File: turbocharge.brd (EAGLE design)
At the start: 56.2 x 21 mm, 69 parts, among them Q01 NMOS40V_10A, Q03 NMOS40V_10A, Q11 PMOS30V_11A, Q12 PMOS30V_11A, Q13 2PMOS30V_2A, Q15 PMOS30V_11A, Q16 PMOS30V_11A, Q21 PMOS30V_11A, Q22 PMOS30V_11A, Q23 PMOS30V_11A, Q25 PMOS30V_11A, Q26 PMOS30V_11A, Q27 PMOS30V_11A, Q28 PMOS30V_11A, Q31 PMOS30V_11A, Q32 PMOS30V_11A, Q33 PMOS30V_11A, Q34 PMOS30V_11A, Q35 PMOS30V_11A, Q36 PMOS30V_11A, Q37 PMOS30V_11A, Q38 PMOS30V_11A, Q41 PMOS30V_11A, Q42 PMOS30V_11A, Q43 PMOS30V_11A, Q44 PMOS30V_11A, Q45 PMOS30V_11A, Q46 PMOS30V_11A, Q47 PMOS30V_11A, Q48 PMOS30V_11A, Q51 PMOS30V_11A, Q52 PMOS30V_11A, Q53 PMOS30V_11A, Q54 PMOS30V_11A, Q55 PMOS30V_11A, Q56 PMOS30V_11A, Q57 PMOS30V_11A, Q58 PMOS30V_11A, Q62 PMOS30V_11A, Q64 PMOS30V_11A, Q66 PMOS30V_11A, Q68 PMOS30V_11A, U1 ATTINY13A10M1, U2 DG408DVZ, U3 CCR20MA_45V

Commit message: .
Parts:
- removed D4, DG1: 4DSCH30V_0A1, dubec:8-HMD
- removed R11, R12: RES100K_16, dubec:0402
- added D6: 3D_SCHOTTKY30V_0.35V, dubec:SOT-363
- added Q17: 2PMOS50V_0.17A, dubec:SOT-666
- added RG11, RG21-: RES100K_16, dubec:0402
- D2: value 3D_SCHOTTKY30V_0.35V -> 4DSCH30V_0A1; device dubec:SOT-363 -> dubec:8-HMD
- Q11, Q12, Q23: value PMOS30V_11A -> NMOS40V_10A
- Q13: value 2PMOS30V_2A -> NMOS40V_10A; device dubec:6-TSOP -> dubec:6-POWERWDFN
- moved D2 66.6 mm to (4.40, 14.8), turned to 0 degrees
- moved Q13 50.5 mm to (21.1, 2.60), turned to 180 degrees
- moved Q01 28.2 mm to (0.00, -16.0), turned to 0 degrees
- moved Q23 26.5 mm to (0.00, -13.8), turned to 0 degrees
- moved Q15 8.00 mm to (17.2, 5.10)
- moved Q16 7.88 mm to (19.9, 5.10)
- moved Q32 2.07 mm to (13.7, 10.5)
- moved Q52 2.07 mm to (13.7, 15.5)
- moved Q31 2.00 mm to (11.0, 10.5)
- moved Q51 2.00 mm to (11.0, 15.5)
- moved Q12 0.57 mm to (13.7, 5.50)
- moved Q22 0.07 mm to (13.7, 8.00)
- moved Q42 0.07 mm to (13.7, 13.0)
- moved Q62 0.07 mm to (13.7, 18.0)
- renumbered RG21 to RG21+, U$2 to T1
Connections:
- removed net G21: D3.5, DG1.7, Q21.G, Q22.G, Q23.G, RG21+.2, U2.6
- removed net N$17: Q12.G, Q13.6, R12.2
- removed net N$18: DG1.1, DG1.2, Q11.G
- new net C4+: D1.4, D1.6, D1.7, D1.8, Q17.1, RG11.1
- new net G21+: D3.5, Q17.2, Q21.G, Q22.G, RG21+.2, U2.6
- new net G21-: Q01.G, Q17.6, Q23.G, RG21-.2
- new net S+11: Q11.S, Q12.S
- net BATT+: now also D2.5, D2.6; no longer D1.6, D1.7, D1.8, D4.6
- net BATT-: now also Q13.S, RG21-.1; no longer Q01.S, R12.1
- net C1: now also Q17.4, Q23.D; no longer Q13.2, Q13.5
- net C2: no longer R11.1
- net C5: now also D2.4; no longer D1.4
- net C6: now also D2.3; no longer D4.3
- net G02: now also Q17.3; no longer Q13.4
- net G11: now also Q11.G, Q12.G, Q13.G, RG11.2; no longer DG1.8, Q01.G, Q13.1, R11.2
- net G13: now also Q17.5; no longer Q13.3
- net G41: now also D6.4; no longer D2.4
- net G51: now also D6.5; no longer D2.5
- net G61: now also D6.6; no longer D2.6
- net N$12: now also D6.2; no longer D2.2
- net N$13: now also D6.3; no longer D2.3
- net N$8: now also D6.1; no longer D2.1
- net S+: now also D2.1, D2.2; no longer D4.1, D4.2
- net S-: now also Q13.D; no longer Q23.D
- net S-21: now also Q01.S; no longer Q11.S, Q12.S
- net VCC: now also D2.7, D2.8; no longer D4.7, D4.8
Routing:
- net S+: track 0.00 -> 12.5 mm
- net C6: track 0.00 -> 4.97 mm
- net S-21: track 3.25 -> 0.00 mm, vias 4 -> 0
- net C5: track 0.00 -> 2.70 mm
- net C4: track 0.00 -> 2.70 mm
- net C3: track 0.00 -> 2.70 mm
- net C2: track 0.00 -> 2.70 mm
- net C1: track 0.00 -> 2.70 mm
- net G51: track 0.00 -> 1.00 mm
- net G41: track 0.00 -> 1.00 mm
- net G31: track 0.00 -> 1.00 mm
- net G21+: track 0.00 -> 1.00 mm, vias 0 -> 2
- net G11: track 0.00 -> 1.00 mm, vias 0 -> 2
- net G61: track 0.00 -> 0.50 mm, vias 2 -> 1
- net N$18: track 0.48 -> 0.00 mm, vias 1 -> 0
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
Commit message: Modularizing next
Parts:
- moved Q15 1.01 mm to (16.3, 5.50)
- moved Q16 0.89 mm to (19.1, 5.50)
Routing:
- net C1: track 2.70 -> 14.6 mm, vias 0 -> 3
- net G21+: track 1.00 -> 3.00 mm
- net G41: track 1.00 -> 3.00 mm
- net G31: track 1.00 -> 3.00 mm
- net G51: track 1.00 -> 3.00 mm
- net G11: track 1.00 -> 2.36 mm
- net S+11: track 0.00 -> 1.28 mm
- added copper zone on layer 15, net BATT-
- added copper zone on layer 2, net BATT-

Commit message: .
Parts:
- moved Q01 29.8 mm to (20.7, 5.50), turned to 180 degrees
- moved Q23 26.4 mm to (18.0, 5.50)
- moved RG21- 26.0 mm to (12.2, 2.60)
- moved RG11 24.0 mm to (4.40, 5.40)
- moved Q15 9.00 mm to (25.3, 5.50)
- moved Q16 9.00 mm to (28.1, 5.50)
- moved R1 2.01 mm to (17.2, 2.60)
- moved Q33 0.72 mm to (18.0, 8.00)
- moved Q43 0.72 mm to (18.0, 10.5)
- moved Q53 0.72 mm to (18.0, 13.0)
- moved Q34 0.62 mm to (20.7, 8.00)
- moved Q44 0.62 mm to (20.7, 10.5)
- moved Q54 0.62 mm to (20.7, 13.0)
- moved Q64 0.62 mm to (20.7, 15.5)
- moved Q13 0.62 mm to (20.7, 3.00)
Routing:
- net C1: track 14.6 -> 23.6 mm
- net G11: track 2.36 -> 3.00 mm

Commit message: .
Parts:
- removed D3, D6: 3D_SCHOTTKY30V_0.35V, dubec:SOT-363
- removed Q01, Q03, Q13: NMOS40V_10A, dubec:6-POWERWDFN
- removed Q15: PMOS30V_11A, dubec:6-POWERWDFN
- removed Q17: 2PMOS50V_0.17A, dubec:SOT-666
- removed R7: RES100K_16, dubec:0402
- removed U2: DG408DVZ, dubec:16-TSSOP
- added Q1, Q14, Q18, Q2, Q24: NMOS40V_10A, dubec:6-POWERWDFN
- added RGT+2, RGT-2, RGT1, RGT3, RGT4, RGT5, RGT6: RES100K_16, dubec:0402
- added U$2, U$3, U$4, U$5, U$6, U$7, U4: 2NMOS30V_0.1A, dubec:SOT-666
- Q16: value PMOS30V_11A -> 2PMOS50V_0.17A; device dubec:6-POWERWDFN -> dubec:SOT-666
- Q27, Q28: value PMOS30V_11A -> NMOS40V_10A
- moved Q16 43.1 mm to (69.8, 16.2), turned to 0 degrees
- moved Q27 4.02 mm to (27.2, 5.50)
- moved Q37 4.02 mm to (27.2, 8.00)
- moved Q47 4.02 mm to (27.2, 10.5)
- moved Q57 4.02 mm to (27.2, 13.0)
- moved Q28 3.90 mm to (29.9, 5.50)
- moved Q38 3.90 mm to (29.9, 8.00)
- moved Q48 3.90 mm to (29.9, 10.5)
- moved Q58 3.90 mm to (29.9, 13.0)
- moved Q68 3.90 mm to (29.9, 15.5)
- moved Q25 3.42 mm to (21.8, 8.00)
- moved Q35 3.42 mm to (21.8, 10.5)
- moved Q45 3.42 mm to (21.8, 13.0)
- moved Q55 3.42 mm to (21.8, 15.5)
- moved Q26 3.30 mm to (24.5, 8.00)
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- renumbered RG11 to RGS1, RG21+ to RGS+2, RG21- to RGS-2, RG31 to RGS3, RG41 to RGS4, RG51 to RGS5, RG61 to RGS6
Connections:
- net S+11 renamed SS+1
- net S+21 renamed SS+2
- net S+22 renamed ST+2
- net S+31 renamed SS+3
- net S+32 renamed ST+3
- net S+41 renamed SS+4
- net S+42 renamed ST+4
- net S+51 renamed SS+5
- net S+52 renamed ST+5
- net S-22 renamed ST-2
- net S-31 renamed SS-3
- net S-32 renamed ST-3
- net S-41 renamed SS-4
- net S-42 renamed ST-4
- net S-51 renamed SS-5
- net S-52 renamed ST-5
- removed net G02: Q03.G, Q17.3, R7.2
- removed net G11: D3.4, Q11.G, Q12.G, Q13.G, RGS1.2, U2.5
- removed net G13: Q15.G, Q16.G, Q17.5
- removed net G21+: D3.5, Q17.2, Q21.G, Q22.G, RGS+2.2, U2.6
- removed net G21-: Q01.G, Q17.6, Q23.G, RGS-2.2
- removed net G22: Q25.G, Q26.G, Q27.G, Q28.G
- removed net G31: D3.6, Q31.G, Q32.G, Q33.G, Q34.G, RGS3.2, U2.7
- removed net G32: Q35.G, Q36.G, Q37.G, Q38.G
- removed net G41: D6.4, Q41.G, Q42.G, Q43.G, Q44.G, RGS4.2, U2.12
- removed net G42: Q45.G, Q46.G, Q47.G, Q48.G
- removed net G51: D6.5, Q51.G, Q52.G, Q53.G, Q54.G, RGS5.2, U2.11
- removed net G52: Q55.G, Q56.G, Q57.G, Q58.G
- removed net G61: D6.6, Q62.G, Q64.G, RGS6.2, U2.10
- removed net G62: Q66.G, Q68.G
- removed net N$10: U2.16
- removed net N$11: U2.1
- removed net N$12: D51.C, D6.2
- removed net N$8: D6.1, D61.C
- removed net N$9: U2.15
- removed net S+12: Q15.S, Q16.S
- removed net S-21: Q01.S, Q23.S
- new net !EN_S1: U4.5
- new net EN_S2: U4.2
- new net EN_S3: U$2.2
- new net EN_S4: U$2.5
- new net EN_S5: U$3.2
- new net EN_S6: U$3.5
- new net EN_T1: U$4.2
- new net EN_T2: U$4.5, U$5.2
- new net EN_T3: U$5.5
- new net EN_T4: U$6.2
- new net EN_T5: U$6.5
- new net EN_T6: U$7.2
- new net GS+2: Q16.2, Q21.G, Q22.G, RGS+2.2, U4.6
- new net GS-2: Q16.6, Q23.G, Q24.G, RGS-2.2
- new net GS1: Q11.G, Q12.G, Q14.G, RGS1.2, U4.3
- new net GS3: Q31.G, Q32.G, Q33.G, Q34.G, RGS3.2, U$2.6
- new net GS4: Q41.G, Q42.G, Q43.G, Q44.G, RGS4.2, U$2.3
- new net GS5: Q51.G, Q52.G, Q53.G, Q54.G, RGS5.2, U$3.6
- new net GS6: Q62.G, Q64.G, RGS6.2, U$3.3
- new net GT+2: Q25.G, Q26.G, RGT+2.2, U$5.6
- new net GT-2: Q27.G, Q28.G, RGT-2.2, U$4.4
- new net GT1: Q1.G, Q18.G, Q2.G, RGT1.2, U$4.1
- new net GT3: Q35.G, Q36.G, Q37.G, Q38.G, RGT3.2, U$5.3
- new net GT4: Q45.G, Q46.G, Q47.G, Q48.G, RGT4.2, U$6.6
- new net GT5: Q55.G, Q56.G, Q57.G, Q58.G, RGT5.2, U$6.3
- new net GT6: Q66.G, Q68.G, RGT6.2, U$7.6
- new net SS-2: Q23.S, Q24.S
- new net ST+1: Q1.S, Q2.S
- net BATT+: now also RGT+2.1, RGT3.1, RGT4.1, RGT5.1, RGT6.1; no longer U2.13
- net BATT-: now also Q14.S, Q18.S, RGT-2.1, RGT1.1, U$2.1, U$2.4, U$3.1, U$3.4, U$5.1, U$5.4, U$6.1, U$6.4, U$7.1, U4.1, U4.4; no longer Q03.S, Q13.S, R7.1, U2.4
- net C1: now also Q1.D; no longer Q15.D, Q17.4
- net C4+: now also Q16.1, U$4.3, U$4.6; no longer Q17.1
- net N$13: no longer D6.3
- net N$14: no longer D3.1
- net N$15: no longer D3.2
- net N$16: no longer D3.3
- net S-: now also Q14.D, Q24.D; no longer Q01.D, Q13.D
- net T+: now also Q2.D; no longer Q16.D
- net T-: now also Q18.D; no longer Q03.D
- net VCC: no longer U2.2
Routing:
- net C1: track 23.6 -> 33.3 mm, vias 3 -> 9
- net G11: track 3.00 -> 0.00 mm, vias 2 -> 0
- net GS1: track 0.00 -> 3.00 mm, vias 0 -> 2
- net G21+: track 3.00 -> 0.00 mm, vias 2 -> 0
- net GS-2: track 0.00 -> 3.00 mm, vias 0 -> 2
- net G41: track 2.60 -> 0.00 mm, vias 2 -> 0
- net G31: track 2.60 -> 0.00 mm, vias 2 -> 0
- net G51: track 2.60 -> 0.00 mm, vias 2 -> 0
- net GS4: track 0.00 -> 1.91 mm, vias 0 -> 2
- net GS3: track 0.00 -> 1.91 mm, vias 0 -> 2
- net GS+2: track 0.00 -> 1.91 mm, vias 0 -> 2
- net GS5: track 0.00 -> 1.91 mm, vias 0 -> 2
- net SS-2: track 0.00 -> 1.27 mm
- net G61: track 0.50 -> 0.00 mm, vias 1 -> 0

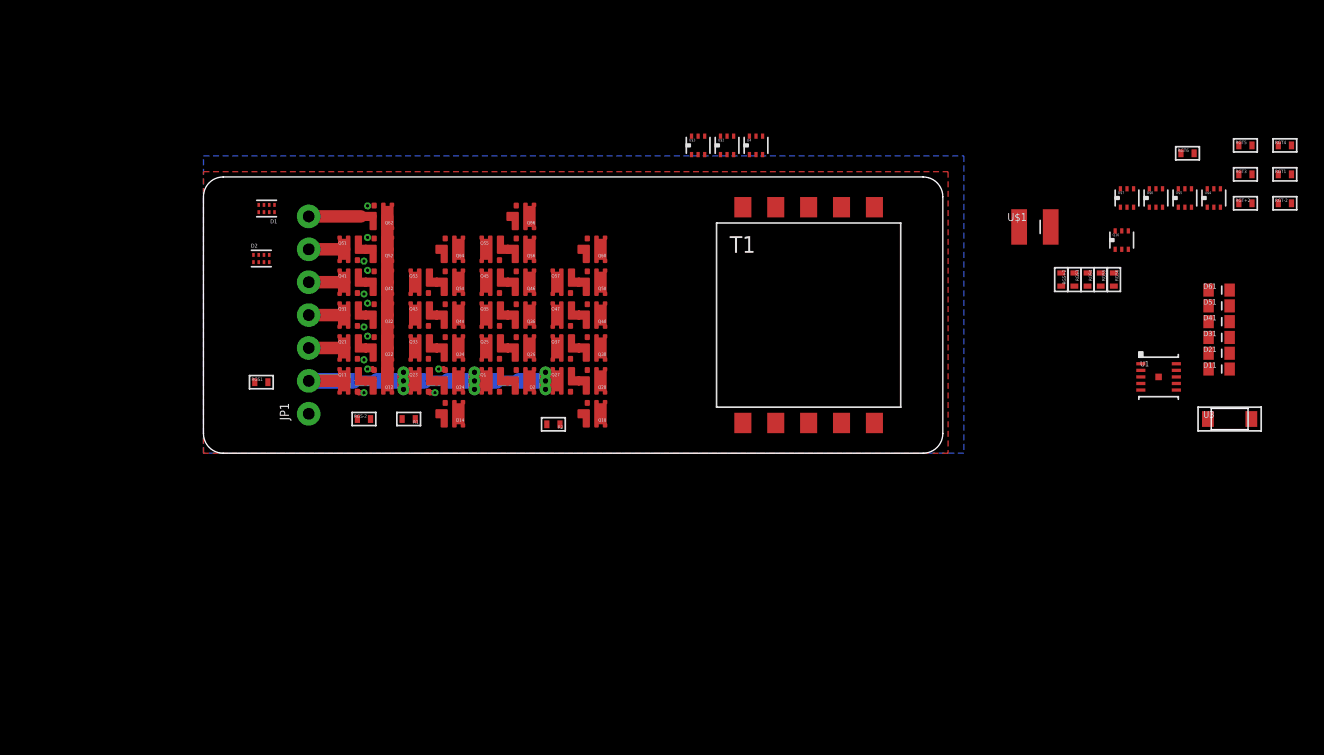
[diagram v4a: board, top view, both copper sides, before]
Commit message: Switching back to an analog switch
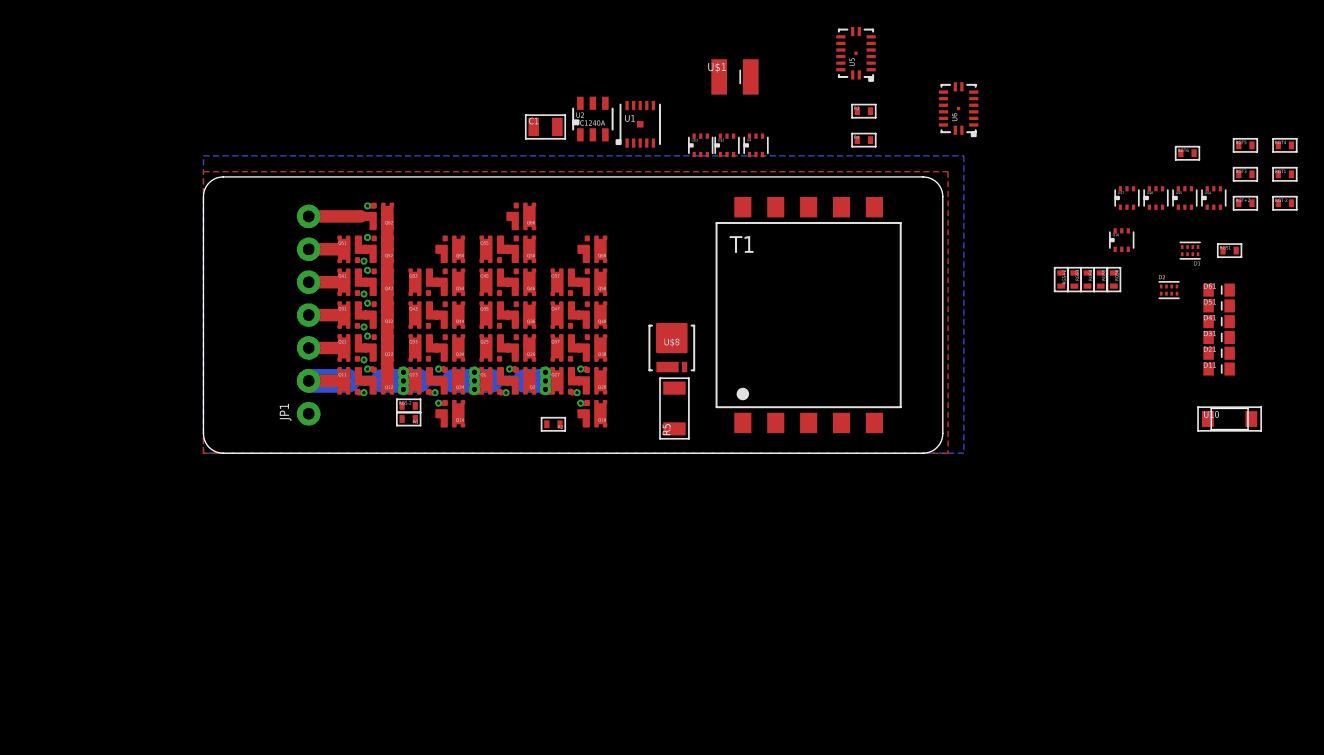
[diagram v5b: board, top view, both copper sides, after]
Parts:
- added C1: (no value), dubec:0805
- added R3, R4: RES4.7K_16, dubec:0402
- added R5: RES01_0.75W, dubec:1206
- added U$8: NMOS30V_30A, dubec:8-POWERWDFN
- added U2: TC1240A, dubec:SOT-23-6
- added U5, U6: 74HC595, dubec:16-VFQFN
- U1: value ATTINY13A10M1 -> LT3757IDD; device dubec:10-MLF -> dubec:10-WFDFN
- moved RGS1 74.3 mm to (78.0, 15.4)
- moved D1 70.3 mm to (75.0, 15.4)
- moved D2 69.0 mm to (73.4, 12.4)
- moved U1 43.8 mm to (33.2, 25.0)
- moved U$1 25.5 mm to (40.4, 28.6)
- moved RGS-2 3.54 mm to (15.6, 3.60)
- moved U$3 0.20 mm to (37.8, 23.4)
- renumbered U3 to U10
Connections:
- net N$2 renamed FBX
- removed net N$6: U1.7
- new net !OE: R3.2, U5.13, U6.13
- new net !RESET: R4.2, U5.10, U6.10
- new net CP: U5.11, U5.12, U6.11, U6.12
- new net DSS: U5.14
- new net DST: U5.9, U6.14
- new net N$10: T1.6, T1.7, U$8.D
- new net N$11: U1.10, U1.8, U1.9, U2.5
- new net N$19: U6.9
- new net N$2: U5.6
- new net N$20: U5.7
- new net N$8: C1.2, U2.6
- new net N$9: C1.1, U2.3
- new net T~: T1.3
- net !EN_S1: now also U5.15
- net BATT-: now also R4.1, U$1.C, U5.8, U5.PAD, U6.8, U6.PAD
- net C1: now also D2.1, D2.2
- net EN_S2: now also U5.1
- net EN_S3: now also U5.2
- net EN_S4: now also U5.3
- net EN_S5: now also U5.4
- net EN_S6: now also U5.5
- net EN_T1: now also U6.15
- net EN_T2: now also U6.1
- net EN_T3: now also U6.2
- net EN_T4: now also U6.3
- net EN_T5: now also U6.4
- net EN_T6: now also U6.5
- net N$1: now also U6.7; no longer U1.4
- net N$3: now also U6.6; no longer U1.1
- net N$5: now also U$8.G, U1.7; no longer U1.9
- net N$7: now also R5.2, U$8.S
- net S+: now also T1.10, T1.9, U2.1; no longer D2.1, D2.2
- net S-: now also R5.1, U1.PAD, U2.2, U2.4; no longer U$1.C, U1.11
- net T-: now also T1.1, T1.4
- net VCC: now also R3.1, U5.16, U6.16; no longer U1.10
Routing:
- net GT1: track 0.00 -> 9.50 mm, vias 0 -> 3
- net GS1: track 3.00 -> 9.50 mm, vias 2 -> 3
- net GT-2: track 0.00 -> 3.00 mm, vias 0 -> 2
- net C1: track 33.3 -> 31.2 mm
- net ST-2: track 0.00 -> 1.28 mm
- net ST+1: track 0.00 -> 1.27 mm
- net GS6: track 0.00 -> 0.50 mm
- added copper zone on layer 1, net C1
